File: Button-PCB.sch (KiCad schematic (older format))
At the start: 32 parts, among them J1 VPP, J10 Strip 4, J11 3V3, J2 UART, J3 Strip 1, J4 Strip 3, J5 RES, J6 5V, J7 Button, J8 Power IN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

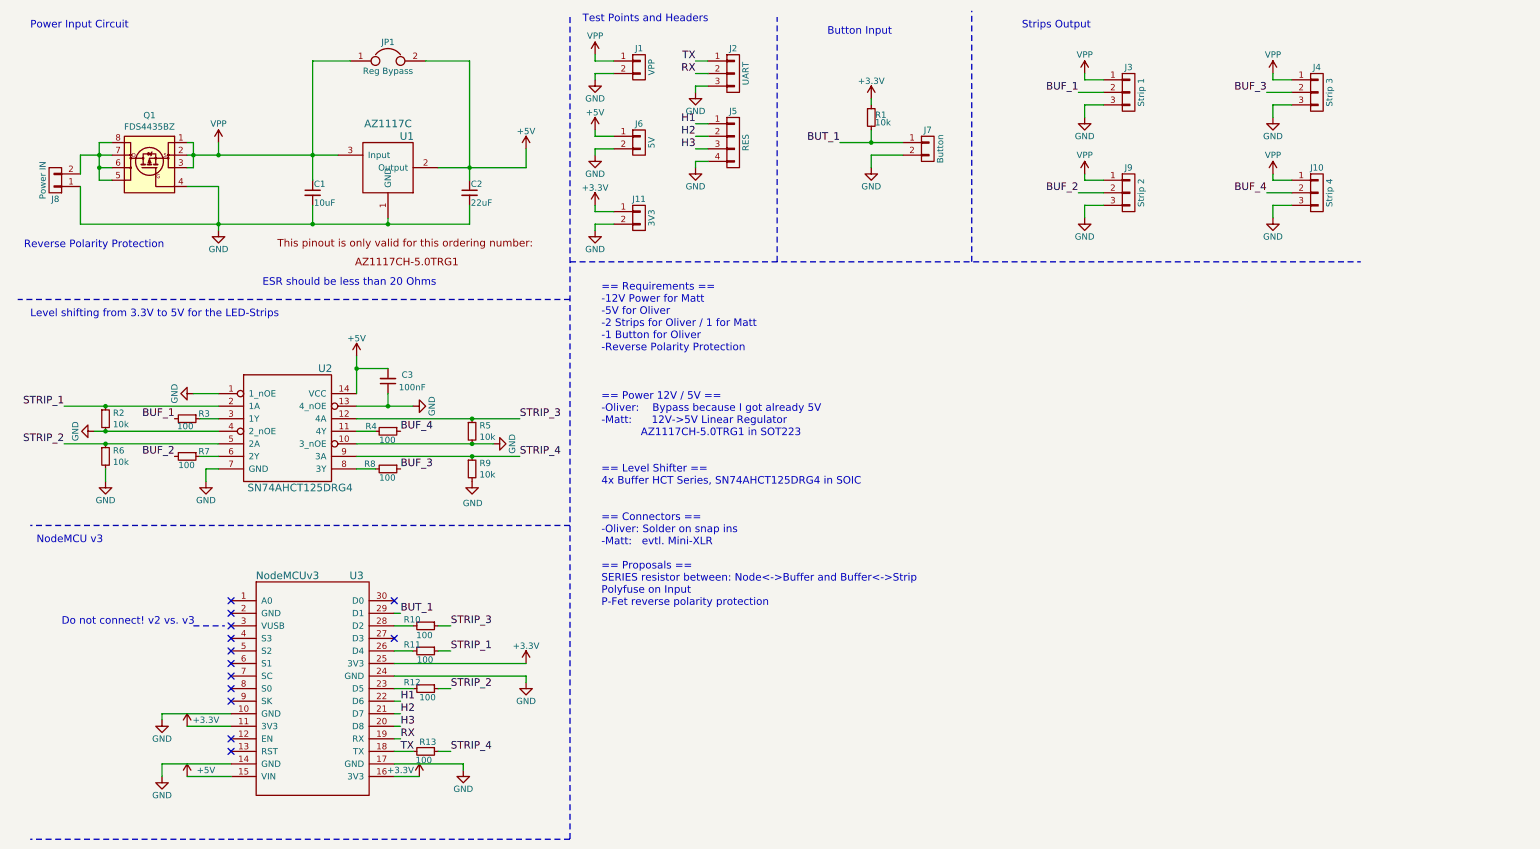
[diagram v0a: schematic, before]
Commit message: Relocating pull-down resistors for easier routing
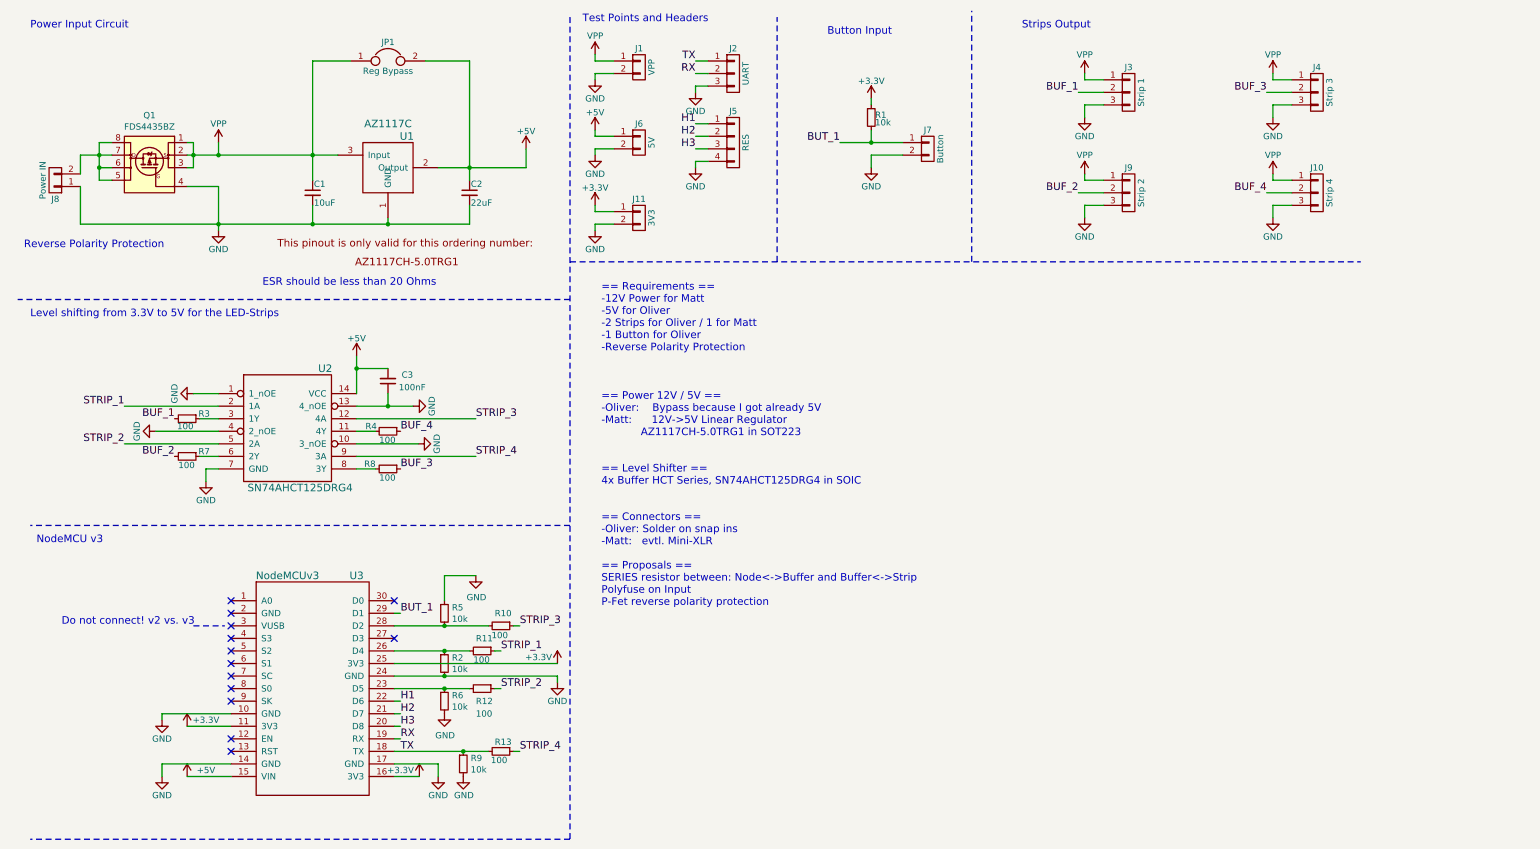
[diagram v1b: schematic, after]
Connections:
- net GND: now also R5.1; no longer R5.2
- net STRIP_1: no longer R2.1
- net STRIP_2: no longer R6.1
- net STRIP_3: no longer R5.1
- net STRIP_4: no longer R9.1
- net TX: now also R9.1
- net at R12.2, U3.23 (D5): now also R6.1
- net at R11.2, U3.26 (D4): now also R2.1
- net at R10.2, U3.28 (D2): now also R5.2
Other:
- moved on the sheet: R10, R11, R12, R13, R2, R5, R6, R9

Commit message: Fixed assignment of footprint for AZ1117C part.
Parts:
- removed J6: 5V, Pin_Headers:Pin_Header_Straight_1x02_Pitch2.54mm, symbol CONN_01X02
- removed U1: AZ1117C, TO_SOT_Packages_SMD:SOT-223-3Lead_TabPin2, symbol AZ1117C
- added U?: AZ1117C, TO_SOT_Packages_SMD:SOT-223-3Lead_TabPin2, symbol AZ1117C
- J1: footprint Pin_Headers:Pin_Header_Straight_1x02_Pitch2.54mm -> Pin_Headers:Pin_Header_Straight_1x04_Pitch2.54mm; symbol CONN_01X02 -> CONN_01X04
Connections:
- net +5V: now also J1.2 (P2), U?.2 (Output)
- net GND: now also J1.3 (P3), J1.4 (P4), U?.1 (GND); no longer J1.2 (P2)
- net VPP: now also U?.3 (Input)
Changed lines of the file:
@@
 EESchema Schematic File Version 2
+LIBS:Button-PCB-rescue
 LIBS:power
 LIBS:device
@@
 H3
 $Comp
-L CONN_01X02 J6
-U 1 1 593F4EB3
-P 5450 1550
-F 0 "J6" H 5450 1700 50  0000 C CNN
-F 1 "5V" V 5550 1550 50  0000 C CNN
-F 2 "Pin_Headers:Pin_Header_Straight_1x02_Pitch2.54mm" H 5450 1550 50  0001 C CNN
-F 3 "" H 5450 1550 50  0001 C CNN
-	1    5450 1550
-	1    0    0    -1
-$EndComp
-$Comp
 L CONN_01X02 J11
 U 1 1 593F4F3B
@@
 $EndComp
 $Comp
-L CONN_01X02 J1
+L CONN_01X04 J1
 U 1 1 593F4F83
-P 5450 950
-F 0 "J1" H 5450 1100 50  0000 C CNN
-F 1 "VPP" V 5550 950 50  0000 C CNN
-F 2 "Pin_Headers:Pin_Header_Straight_1x02_Pitch2.54mm" H 5450 950 50  0001 C CNN
-F 3 "" H 5450 950 50  0001 C CNN
-	1    5450 950
+P 5450 1050
+F 0 "J1" H 5450 1300 50  0000 C CNN
+F 1 "VPP" V 5550 1050 50  0000 C CNN
+F 2 "Pin_Headers:Pin_Header_Straight_1x04_Pitch2.54mm" H 5450 1050 50  0001 C CNN
+F 3 "" H 5450 1050 50  0001 C CNN
+	1    5450 1050
 	1    0    0    -1
 $EndComp
@@
 L VPP #PWR019
 U 1 1 593F534F
-P 5100 850
-F 0 "#PWR019" H 5100 700 50  0001 C CNN
-F 1 "VPP" H 5100 1000 50  0000 C CNN
-F 2 "" H 5100 850 50  0001 C CNN
-F 3 "" H 5100 850 50  0001 C CNN
-	1    5100 850
+P 5200 850
+F 0 "#PWR019" H 5200 700 50  0001 C CNN
+F 1 "VPP" H 5200 1000 50  0000 C CNN
+F 2 "" H 5200 850 50  0001 C CNN
+F 3 "" H 5200 850 50  0001 C CNN
+	1    5200 850
 	1    0    0    -1
 $EndComp
@@
 L +5V #PWR021
 U 1 1 593F5B1E
-P 5100 1450
-F 0 "#PWR021" H 5100 1300 50  0001 C CNN
-F 1 "+5V" H 5100 1590 50  0000 C CNN
-F 2 "" H 5100 1450 50  0001 C CNN
-F 3 "" H 5100 1450 50  0001 C CNN
-	1    5100 1450
+P 5100 1000
+F 0 "#PWR021" H 5100 850 50  0001 C CNN
+F 1 "+5V" H 5100 1140 50  0000 C CNN
+F 2 "" H 5100 1000 50  0001 C CNN
+F 3 "" H 5100 1000 50  0001 C CNN
+	1    5100 1000
 	1    0    0    -1
 $EndComp
@@
 L GND #PWR022
 U 1 1 593F5D64
-P 5100 1050
-F 0 "#PWR022" H 5100 800 50  0001 C CNN
-F 1 "GND" H 5100 900 50  0000 C CNN
-F 2 "" H 5100 1050 50  0001 C CNN
-F 3 "" H 5100 1050 50  0001 C CNN
-	1    5100 1050
+P 5100 1200
+F 0 "#PWR022" H 5100 950 50  0001 C CNN
+F 1 "GND" H 5100 1050 50  0000 C CNN
+F 2 "" H 5100 1200 50  0001 C CNN
+F 3 "" H 5100 1200 50  0001 C CNN
+	1    5100 1200
 	1    0    0    -1
 $EndComp
 $Comp
 L GND #PWR023
-U 1 1 593F5F98
-P 5100 1650
-F 0 "#PWR023" H 5100 1400 50  0001 C CNN
-F 1 "GND" H 5100 1500 50  0000 C CNN
-F 2 "" H 5100 1650 50  0001 C CNN
-F 3 "" H 5100 1650 50  0001 C CNN
-	1    5100 1650
-	1    0    0    -1
-$EndComp
-$Comp
-L GND #PWR024
 U 1 1 593F6043
 P 5100 2250
-F 0 "#PWR024" H 5100 2000 50  0001 C CNN
+F 0 "#PWR023" H 5100 2000 50  0001 C CNN
 F 1 "GND" H 5100 2100 50  0000 C CNN
 F 2 "" H 5100 2250 50  0001 C CNN
@@
 Test Points and Headers
 $Comp
-L AZ1117C U1
-U 1 1 593F7393
-P 3650 2000
-F 0 "U1" H 3600 2500 60  0000 C CNN
-F 1 "AZ1117C" H 3450 2600 60  0000 C CNN
-F 2 "TO_SOT_Packages_SMD:SOT-223-3Lead_TabPin2" H 3650 2000 60  0001 C CNN
-F 3 "" H 3650 2000 60  0001 C CNN
-	1    3650 2000
-	1    0    0    -1
-$EndComp
-$Comp
-L +5V #PWR025
+L +5V #PWR024
 U 1 1 593F7638
 P 4550 1600
-F 0 "#PWR025" H 4550 1450 50  0001 C CNN
+F 0 "#PWR024" H 4550 1450 50  0001 C CNN
 F 1 "+5V" H 4550 1740 50  0000 C CNN
 F 2 "" H 4550 1600 50  0001 C CNN
@@
 ESR should be less than 20 Ohms
 $Comp
-L GND #PWR026
+L GND #PWR025
 U 1 1 593F7ACE
 P 2100 2250
-F 0 "#PWR026" H 2100 2000 50  0001 C CNN
+F 0 "#PWR025" H 2100 2000 50  0001 C CNN
 F 1 "GND" H 2100 2100 50  0000 C CNN
 F 2 "" H 2100 2250 50  0001 C CNN
@@
 $EndComp
 $Comp
-L VPP #PWR027
+L VPP #PWR026
 U 1 1 593F9797
 P 2100 1550
-F 0 "#PWR027" H 2100 1400 50  0001 C CNN
+F 0 "#PWR026" H 2100 1400 50  0001 C CNN
 F 1 "VPP" H 2100 1700 50  0000 C CNN
 F 2 "" H 2100 1550 50  0001 C CNN
@@
 $EndComp
 $Comp
-L GND #PWR028
+L GND #PWR027
 U 1 1 5942C149
 P 2000 4250
-F 0 "#PWR028" H 2000 4000 50  0001 C CNN
+F 0 "#PWR027" H 2000 4000 50  0001 C CNN
 F 1 "GND" H 2000 4100 50  0000 C CNN
 F 2 "" H 2000 4250 50  0001 C CNN
@@
 $EndComp
 $Comp
-L GND #PWR029
+L GND #PWR028
 U 1 1 5942C449
 P 3650 3650
-F 0 "#PWR029" H 3650 3400 50  0001 C CNN
+F 0 "#PWR028" H 3650 3400 50  0001 C CNN
 F 1 "GND" H 3650 3500 50  0000 C CNN
 F 2 "" H 3650 3650 50  0001 C CNN
@@
 $EndComp
 $Comp
-L GND #PWR030
+L GND #PWR029
 U 1 1 5942C499
 P 3690 3950
-F 0 "#PWR030" H 3690 3700 50  0001 C CNN
+F 0 "#PWR029" H 3690 3700 50  0001 C CNN
 F 1 "GND" H 3690 3800 50  0000 C CNN
 F 2 "" H 3690 3950 50  0001 C CNN
@@
 BUF_4
 $Comp
-L GND #PWR031
+L GND #PWR030
 U 1 1 5942E71C
 P 1600 3850
-F 0 "#PWR031" H 1600 3600 50  0001 C CNN
+F 0 "#PWR030" H 1600 3600 50  0001 C CNN
 F 1 "GND" H 1600 3700 50  0000 C CNN
 F 2 "" H 1600 3850 50  0001 C CNN
@@
 $EndComp
 $Comp
-L GND #PWR032
+L GND #PWR031
 U 1 1 5942EAC2
 P 1900 3550
-F 0 "#PWR032" H 1900 3300 50  0001 C CNN
+F 0 "#PWR031" H 1900 3300 50  0001 C CNN
 F 1 "GND" H 1900 3400 50  0000 C CNN
 F 2 "" H 1900 3550 50  0001 C CNN
@@
 $EndComp
 $Comp
-L +5V #PWR033
+L +5V #PWR032
 U 1 1 5942FE36
 P 3200 3250
-F 0 "#PWR033" H 3200 3100 50  0001 C CNN
+F 0 "#PWR032" H 3200 3100 50  0001 C CNN
 F 1 "+5V" H 3200 3390 50  0000 C CNN
 F 2 "" H 3200 3250 50  0001 C CNN
@@
 $EndComp
 $Comp
-L GND #PWR035
+L GND #PWR033
 U 1 1 5945C810
 P 4050 6600
-F 0 "#PWR035" H 4050 6350 50  0001 C CNN
+F 0 "#PWR033" H 4050 6350 50  0001 C CNN
 F 1 "GND" H 4055 6450 50  0000 C CNN
 F 2 "" H 4050 6600 50  0001 C CNN
@@
 	7300 1250 7300 1200
 Wire Wire Line
-	7050 1550 7300 1550
-Wire Wire Line
-	7300 1550 7550 1550
+	7050 1550 7550 1550
 Wire Wire Line
 	7300 1550 7300 1450
 Wire Wire Line
-	3500 5800 3900 5800
-Wire Wire Line
-	3900 5800 4800 5800
+	3500 5800 4800 5800
 Wire Wire Line
 	4800 5800 4800 5850
@@
 	3500 5700 4800 5700
 Wire Wire Line
-	3500 5600 3900 5600
-Wire Wire Line
-	3900 5600 4100 5600
+	3500 5600 4100 5600
 Wire Wire Line
 	3550 5300 3500 5300
 Wire Wire Line
-	3500 6400 4050 6400
-Wire Wire Line
-	4050 6400 4250 6400
-Wire Wire Line
-	3500 5400 3900 5400
-Wire Wire Line
-	3900 5400 4250 5400
-Wire Wire Line
-	3500 5900 3900 5900
-Wire Wire Line
-	3900 5900 4100 5900
+	3500 6400 4250 6400
+Wire Wire Line
+	3500 5400 4250 5400
+Wire Wire Line
+	3500 5900 4100 5900
 Wire Wire Line
 	3500 6000 3550 6000
@@
 	5100 2100 5250 2100
 Wire Wire Line
-	5100 1450 5100 1500
-Wire Wire Line
-	5100 1500 5250 1500
-Wire Wire Line
-	5100 850  5100 900
-Wire Wire Line
-	5100 900  5250 900
+	5200 850  5200 900
 Wire Wire Line
 	5250 1000 5100 1000
-Wire Wire Line
-	5100 1000 5100 1050
-Wire Wire Line
-	5100 1650 5100 1600
-Wire Wire Line
-	5100 1600 5250 1600
 Wire Wire Line
 	5100 2250 5100 2200
@@
 	4900 550  4900 7100
 Wire Wire Line
-	2100 1900 2100 2200
-Wire Wire Line
-	2100 2200 2100 2250
+	2100 1900 2100 2250
 Wire Wire Line
 	4100 2200 4100 2050
@@
 	3450 2200 3450 2150
 Wire Wire Line
-	3850 1750 4100 1750
-Wire Wire Line
-	4100 1750 4550 1750
+	3850 1750 4550 1750
 Wire Wire Line
 	4550 1750 4550 1600
 Wire Wire Line
-	4100 900  4100 1750
-Wire Wire Line
-	4100 1750 4100 1850
+	4100 900  4100 1850
 Connection ~ 4100 1750
 Wire Wire Line
-	1000 2200 2100 2200
-Wire Wire Line
-	2100 2200 2850 2200
-Wire Wire Line
-	2850 2200 3450 2200
-Wire Wire Line
-	3450 2200 4100 2200
+	1000 2200 4100 2200
 Connection ~ 3450 2200
 Wire Wire Line
@@
 Connection ~ 2850 2200
 Wire Wire Line
-	2850 900  2850 1650
-Wire Wire Line
-	2850 1650 2850 1850
+	2850 900  2850 1850
 Wire Wire Line
 	3750 900  4100 900
@@
 	1900 3550 2100 3550
 Wire Wire Line
-	3200 3650 3450 3650
-Wire Wire Line
-	3450 3650 3650 3650
+	3200 3650 3650 3650
 Wire Wire Line
 	3200 3750 4150 3750
@@
 	3450 3350 3200 3350
 Wire Wire Line
-	3200 3250 3200 3350
-Wire Wire Line
-	3200 3350 3200 3550
+	3200 3250 3200 3550
 Connection ~ 3200 3350
 Wire Notes Line
@@
 	1850 1900 2100 1900
 Wire Wire Line
-	1850 1650 1900 1650
-Wire Wire Line
-	1900 1650 2100 1650
-Wire Wire Line
-	2100 1650 2850 1650
-Wire Wire Line
-	2850 1650 3050 1650
+	1850 1650 3050 1650
 Wire Wire Line
 	1850 1550 1900 1550
 Wire Wire Line
-	1900 1550 1900 1650
-Wire Wire Line
-	1900 1650 1900 1750
+	1900 1550 1900 1750
 Connection ~ 1900 1650
 Wire Wire Line
 	1900 1750 1850 1750
 Wire Wire Line
-	1000 1650 1150 1650
-Wire Wire Line
-	1150 1650 1250 1650
-Wire Wire Line
-	1150 1550 1150 1650
-Wire Wire Line
-	1150 1650 1150 1750
-Wire Wire Line
-	1150 1750 1150 1850
+	1000 1650 1250 1650
+Wire Wire Line
+	1150 1550 1150 1850
 Wire Wire Line
 	1150 1550 1250 1550
@@
 Connection ~ 1150 1750
 $Comp
-L GND #PWR036
+L GND #PWR034
 U 1 1 5945DAFF
 P 5900 1750
-F 0 "#PWR036" H 5900 1500 50  0001 C CNN
+F 0 "#PWR034" H 5900 1500 50  0001 C CNN
 F 1 "GND" H 5900 1600 50  0000 C CNN
 F 2 "" H 5900 1750 50  0001 C CNN
@@
 $EndComp
 $Comp
-L GND #PWR037
+L GND #PWR035
 U 1 1 5945DB85
 P 5900 1150
-F 0 "#PWR037" H 5900 900 50  0001 C CNN
+F 0 "#PWR035" H 5900 900 50  0001 C CNN
 F 1 "GND" H 5900 1000 50  0000 C CNN
 F 2 "" H 5900 1150 50  0001 C CNN
@@
 Connection ~ 3900 5900
 $Comp
-L GND #PWR?
+L GND #PWR036
 U 1 1 5946ABBC
 P 3900 6100
-F 0 "#PWR?" H 3900 5850 50  0001 C CNN
+F 0 "#PWR036" H 3900 5850 50  0001 C CNN
 F 1 "GND" H 3905 5927 50  0000 C CNN
 F 2 "" H 3900 6100 50  0001 C CNN
@@
 Connection ~ 3900 5800
 $Comp
-L GND #PWR?
+L GND #PWR037
 U 1 1 5946B5F5
 P 4150 5000
-F 0 "#PWR?" H 4150 4750 50  0001 C CNN
+F 0 "#PWR037" H 4150 4750 50  0001 C CNN
 F 1 "GND" H 4155 4827 50  0000 C CNN
 F 2 "" H 4150 5000 50  0001 C CNN
@@
 Wire Wire Line
 	2100 3950 1350 3950
+Wire Wire Line
+	5200 900  5250 900
+Wire Wire Line
+	5250 1100 5100 1100
+Wire Wire Line
+	5100 1100 5100 1200
+Wire Wire Line
+	5100 1200 5250 1200
+$Comp
+L AZ1117C U?
+U 1 1 594E8EDE
+P 3650 2000
+F 0 "U?" H 3600 2637 60  0000 C CNN
+F 1 "AZ1117C" H 3600 2531 60  0000 C CNN
+F 2 "TO_SOT_Packages_SMD:SOT-223-3Lead_TabPin2" H 3450 1400 60  0001 C CNN
+F 3 "" H 3650 2000 60  0001 C CNN
+	1    3650 2000
+	1    0    0    -1
+$EndComp
 $EndSCHEMATC

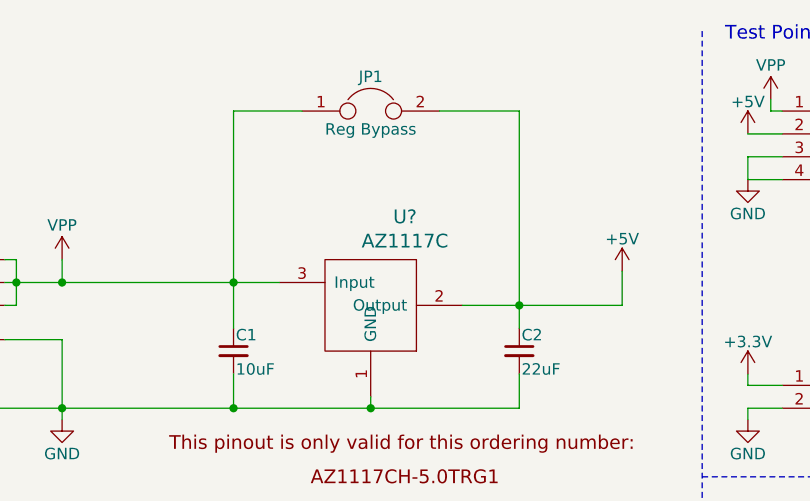
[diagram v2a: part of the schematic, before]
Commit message: Annotate regulator (U1)
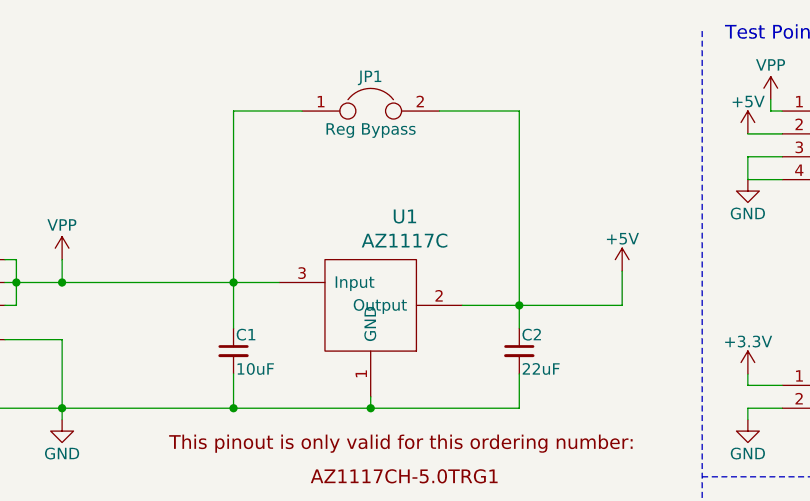
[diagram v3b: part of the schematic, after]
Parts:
- Q1: footprint SMD_Packages:SOIC-8-N -> Housings_SOIC:SOIC-8_3.9x4.9mm_Pitch1.27mm
- gave numbers to parts that had none: 1
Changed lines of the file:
@@
 F 0 "Q1" H 1550 2167 50  0000 C CNN
 F 1 "FDS4435BZ" H 1550 2076 50  0000 C CNN
-F 2 "SMD_Packages:SOIC-8-N" H 1550 1950 50  0001 C CIN
+F 2 "Housings_SOIC:SOIC-8_3.9x4.9mm_Pitch1.27mm" H 1550 1950 50  0001 C CIN
 F 3 "" V 1550 1750 50  0001 L CNN
 	1    1550 1750
@@
 	5100 1200 5250 1200
 $Comp
-L AZ1117C U?
+L AZ1117C U1
 U 1 1 594E8EDE
 P 3650 2000
-F 0 "U?" H 3600 2637 60  0000 C CNN
+F 0 "U1" H 3600 2637 60  0000 C CNN
 F 1 "AZ1117C" H 3600 2531 60  0000 C CNN
 F 2 "TO_SOT_Packages_SMD:SOT-223-3Lead_TabPin2" H 3450 1400 60  0001 C CNN
